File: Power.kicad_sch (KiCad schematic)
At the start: 46 parts, among them J3 DBT50G-9.5-2P, J38 2.54-1*4, J4 DBT50G-9.5-2P, J5 DBT50G-9.5-2P, J6 DBT50G-9.5-2P, U5 TPS63070RNMR

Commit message: Fix ERC: register missing libraries, add PWR_FLAGs, rename zone rails
- Register project-local sym-lib-table/fp-lib-table. PixelBlit points at
  pico-pixel's live library; RPI_COMPILED/KiCad_Standard/EasyEDA/PCM_JLCPCB
  footprints vendored (via the abandoned universal-strip-controller-first
  attempt) into libs/; RPI_DB, RPI - Power, EasyEDA, PCM_JLCPCB-Diodes and
  PCM_JLCPCB-Resistors symbols extracted from the schematics' own embedded
  symbol cache into standalone .kicad_sym files, validated with
  `kicad-cli sym upgrade`.
- Fix U1's footprint: RPI_COMPILED:rpi_rp2350b doesn't exist anywhere
  (not even in the original RP2350B-MINIMAL reference) - corrected to
  rpi_rp2350b_vias, the footprint that's actually there.
- Point D10 (BZT52C15V) and R5/R20 (0603s) at KiCad's own standard
  SOD-123/0603 footprints; no vendored copy of their original
  EasyEDA/JLCPCB footprints existed anywhere to source from.
- Add PWR_FLAGs on the 8 nets ERC found undriven: +VIN_Z1-4, +12V_SYS,
  GND (top sheet), +1V1, and VREG_AVDD (U1 pin 61).
- Rename +12V_Z1-4 to +VIN_Z1-4 (zones carry 5-12V depending on what's
  plugged in, not a fixed 12V).

ERC: 1009 violations / 8 errors -> 533 violations / 0 errors.
Remaining warnings are pre-existing: fuse/diode symbols typed
Unspecified instead of Passive (pin_to_pin), intentional dual net
labels (STRINGn/GPIOn etc., except a real USB_D+/USB_D- issue still
open), schematic drawing hygiene (off-grid/dangling wire endpoints),
and symbol-cache drift now visible now that real libraries exist
(lib_symbol_mismatch - fix via Update Symbols from Library in KiCad).
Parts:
- D10: footprint EasyEDA:SOD-123_L2.7-W1.6-LS3.7-RD-1 -> Diode_SMD:D_SOD-123
- R20, R5: footprint PCM_JLCPCB:R_0603 -> Resistor_SMD:R_0603_1608Metric
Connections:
- net +12V_Z1 renamed +VIN_Z1
- net +12V_Z2 renamed +VIN_Z2
- net +12V_Z3 renamed +VIN_Z3
- net +12V_Z4 renamed +VIN_Z4
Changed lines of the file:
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@@
 			)
 		)
-		(property "Value" "+12V_Z4"
+		(property "Value" "+VIN_Z4"
 			(at 265.684 143.002 0)
 			(show_name no)
@@
 			)
 		)
-		(property "Value" "+12V_Z2"
+		(property "Value" "+VIN_Z2"
 			(at 247.396 143.256 0)
 			(show_name no)
@@
 			)
 		)
-		(property "Value" "+12V_Z2"
+		(property "Value" "+VIN_Z2"
 			(at 180.34 99.06 0)
 			(show_name no)
@@
 			)
 		)
-		(property "Value" "+12V_Z3"
+		(property "Value" "+VIN_Z3"
 			(at 256.54 143.256 0)
 			(show_name no)
@@
 			)
 		)
-		(property "Value" "+12V_Z1"
+		(property "Value" "+VIN_Z1"
 			(at 236.982 143.51 0)
 			(show_name no)
@@
 			)
 		)
-		(property "Value" "+12V_Z2"
+		(property "Value" "+VIN_Z2"
 			(at 267.97 88.392 0)
 			(show_name no)
@@
 			)
 		)
-		(property "Value" "+12V_Z1"
+		(property "Value" "+VIN_Z1"
 			(at 242.57 88.392 0)
 			(show_name no)
@@
 			)
 		)
-		(property "Value" "+12V_Z3"
+		(property "Value" "+VIN_Z3"
 			(at 267.97 103.632 0)
 			(show_name no)
@@
 			)
 		)
-		(property "Value" "+12V_Z3"
+		(property "Value" "+VIN_Z3"
 			(at 242.57 116.332 0)
 			(show_name no)
@@
 			)
 		)
-		(property "Footprint" "EasyEDA:SOD-123_L2.7-W1.6-LS3.7-RD-1"
+		(property "Footprint" "Diode_SMD:D_SOD-123"
 			(at 25.4 50.8 0)
 			(hide yes)
@@
 			)
 		)
-		(property "Value" "+12V_Z4"
+		(property "Value" "+VIN_Z4"
 			(at 180.34 124.46 0)
 			(show_name no)
@@
 			)
 		)
-		(property "Value" "+12V_Z4"
+		(property "Value" "+VIN_Z4"
 			(at 267.97 116.332 0)
 			(show_name no)
@@
 			)
 		)
-		(property "Value" "+12V_Z1"
+		(property "Value" "+VIN_Z1"
 			(at 177.8 87.122 0)
 			(show_name no)
@@
 			)
 		)
-		(property "Footprint" "PCM_JLCPCB:R_0603"
+		(property "Footprint" "Resistor_SMD:R_0603_1608Metric"
 			(at 168.91 52.578 90)
 			(hide yes)
@@
 			)
 		)
-		(property "Value" "+12V_Z2"
+		(property "Value" "+VIN_Z2"
 			(at 242.57 103.632 0)
 			(show_name no)
@@
 	)
 	(symbol
+		(lib_id "PixelBlit:PWR_FLAG")
+		(at 38.1 48.26 90)
+		(unit 1)
+		(body_style 1)
+		(exclude_from_sim no)
+		(in_bom yes)
+		(on_board yes)
+		(in_pos_files yes)
+		(dnp no)
+		(fields_autoplaced yes)
+		(property "Reference" "#FLG23"
+			(at 36.195 48.26 0)
+			(hide yes)
+			(show_name no)
+			(do_not_autoplace no)
+			(effects
+				(font
+					(size 1.27 1.27)
+				)
+			)
+		)
+		(property "Value" "PWR_FLAG"
+			(at 34.29 48.259899999999995 90)
+			(show_name no)
+			(do_not_autoplace no)
+			(effects
+				(font
+					(size 1.27 1.27)
+				)
+				(justify left)
+			)
+		)
+		(property "Footprint" ""
+			(at 38.1 48.26 0)
+			(hide yes)
+			(show_name no)
+			(do_not_autoplace no)
+			(effects
+				(font
+					(size 1.27 1.27)
+				)
+			)
+		)
+		(property "Datasheet" ""
+			(at 38.1 48.26 0)
+			(hide yes)
+			(show_name no)
+			(do_not_autoplace no)
+			(effects
+				(font
+					(size 1.27 1.27)
+				)
+			)
+		)
+		(property "Description" "Special symbol for telling ERC where power comes from"
+			(at 38.1 48.26 0)
+			(hide yes)
+			(show_name no)
+			(do_not_autoplace no)
+			(effects
+				(font
+					(size 1.27 1.27)
+				)
+			)
+		)
+		(pin "1"
+		)
+		(instances
+			(project "universal-strip-controller"
+				(path "/b1a25501-925f-4082-acf3-9513bc59c329/b2bef3cb-9181-478c-9c64-5764e6fff4f7"
+					(reference "#FLG23")
+					(unit 1)
+				)
+			)
+		)
+	)
+	(wire
+		(pts
+			(xy 30.48 48.26) (xy 38.1 48.26)
+		)
+		(stroke
+			(width 0)
+			(type default)
+		)
+	)
+	(symbol
 		(lib_id "PixelBlit:GND")
 		(at 181.61 50.8 0)
@@
 			)
 		)
-		(property "Footprint" "PCM_JLCPCB:R_0603"
+		(property "Footprint" "Resistor_SMD:R_0603_1608Metric"
 			(at 215.9 156.718 90)
 			(hide yes)
@@
 			)
 		)
-		(property "Value" "+12V_Z3"
+		(property "Value" "+VIN_Z3"
 			(at 180.34 111.76 0)
 			(show_name no)
@@
 		)
 	)
+	(symbol
+		(lib_id "PixelBlit:PWR_FLAG")
+		(at 187.96 116.84 90)
+		(unit 1)
+		(body_style 1)
+		(exclude_from_sim no)
+		(in_bom yes)
+		(on_board yes)
+		(in_pos_files yes)
+		(dnp no)
+		(fields_autoplaced yes)
+		(property "Reference" "#FLG24"
+			(at 186.055 116.84 0)
+			(hide yes)
+			(show_name no)
+			(do_not_autoplace no)
+			(effects
+				(font
+					(size 1.27 1.27)
+				)
+			)
+		)
+		(property "Value" "PWR_FLAG"
+			(at 184.15 116.8399 90)
+			(show_name no)
+			(do_not_autoplace no)
+			(effects
+				(font
+					(size 1.27 1.27)
+				)
+				(justify left)
+			)
+		)
+		(property "Footprint" ""
+			(at 187.96 116.84 0)
+			(hide yes)
+			(show_name no)
+			(do_not_autoplace no)
+			(effects
+				(font
+					(size 1.27 1.27)
+				)
+			)
+		)
+		(property "Datasheet" ""
+			(at 187.96 116.84 0)
+			(hide yes)
+			(show_name no)
+			(do_not_autoplace no)
+			(effects
+				(font
+					(size 1.27 1.27)
+				)
+			)
+		)
+		(property "Description" "Special symbol for telling ERC where power comes from"
+			(at 187.96 116.84 0)
+			(hide yes)
+			(show_name no)
+			(do_not_autoplace no)
+			(effects
+				(font
+					(size 1.27 1.27)
+				)
+			)
+		)
+		(pin "1"
+		)
+		(instances
+			(project "universal-strip-controller"
+				(path "/b1a25501-925f-4082-acf3-9513bc59c329/b2bef3cb-9181-478c-9c64-5764e6fff4f7"
+					(reference "#FLG24")
+					(unit 1)
+				)
+			)
+		)
+	)
+	(wire
+		(pts
+			(xy 180.34 116.84) (xy 187.96 116.84)
+		)
+		(stroke
+			(width 0)
+			(type default)
+		)
+	)

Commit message: Updated symbols from library
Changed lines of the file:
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@@
 	(wire
 		(pts
+			(xy 180.34 116.84) (xy 187.96 116.84)
+		)
+		(stroke
+			(width 0)
+			(type default)
+		)
+	)
+	(wire
+		(pts
 			(xy 162.56 50.8) (xy 165.1 50.8)
 		)
@@
 	(wire
 		(pts
+			(xy 30.48 48.26) (xy 38.1 48.26)
+		)
+		(stroke
+			(width 0)
+			(type default)
+		)
+	)
+	(wire
+		(pts
 			(xy 245.11 107.95) (xy 245.11 110.49)
 		)
@@
 	)
 	(symbol
+		(lib_id "PixelBlit:PWR_FLAG")
+		(at 38.1 48.26 90)
+		(unit 1)
+		(body_style 1)
+		(exclude_from_sim no)
+		(in_bom yes)
+		(on_board yes)
+		(in_pos_files yes)
+		(dnp no)
+		(fields_autoplaced yes)
+		(property "Reference" "#FLG23"
+			(at 36.195 48.26 0)
+			(hide yes)
+			(show_name no)
+			(do_not_autoplace no)
+			(effects
+				(font
+					(size 1.27 1.27)
+				)
+			)
+		)
+		(property "Value" "PWR_FLAG"
+			(at 34.29 48.2599 90)
+			(show_name no)
+			(do_not_autoplace no)
+			(effects
+				(font
+					(size 1.27 1.27)
+				)
+				(justify left)
+			)
+		)
+		(property "Footprint" ""
+			(at 38.1 48.26 0)
+			(hide yes)
+			(show_name no)
+			(do_not_autoplace no)
+			(effects
+				(font
+					(size 1.27 1.27)
+				)
+			)
+		)
+		(property "Datasheet" ""
+			(at 38.1 48.26 0)
+			(hide yes)
+			(show_name no)
+			(do_not_autoplace no)
+			(effects
+				(font
+					(size 1.27 1.27)
+				)
+			)
+		)
+		(property "Description" "Special symbol for telling ERC where power comes from"
+			(at 38.1 48.26 0)
+			(hide yes)
+			(show_name no)
+			(do_not_autoplace no)
+			(effects
+				(font
+					(size 1.27 1.27)
+				)
+			)
+		)
+		(pin "1"
+		)
+		(instances
+			(project "universal-strip-controller"
+				(path "/b1a25501-925f-4082-acf3-9513bc59c329/b2bef3cb-9181-478c-9c64-5764e6fff4f7"
+					(reference "#FLG23")
+					(unit 1)
+				)
+			)
+		)
+	)
+	(symbol
 		(lib_id "PixelBlit:+5V")
 		(at 30.48 130.81 0)
@@
 	(symbol
 		(lib_id "PixelBlit:PWR_FLAG")
-		(at 38.1 48.26 90)
+		(at 187.96 116.84 90)
 		(unit 1)
 		(body_style 1)
@@
 		(dnp no)
 		(fields_autoplaced yes)
-		(property "Reference" "#FLG23"
-			(at 36.195 48.26 0)
+		(property "Reference" "#FLG24"
+			(at 186.055 116.84 0)
 			(hide yes)
 			(show_name no)
@@
 		)
 		(property "Value" "PWR_FLAG"
-			(at 34.29 48.259899999999995 90)
+			(at 184.15 116.8399 90)
 			(show_name no)
 			(do_not_autoplace no)
@@
 		)
 		(property "Footprint" ""
-			(at 38.1 48.26 0)
+			(at 187.96 116.84 0)
 			(hide yes)
 			(show_name no)
@@
 		)
 		(property "Datasheet" ""
-			(at 38.1 48.26 0)
+			(at 187.96 116.84 0)
 			(hide yes)
 			(show_name no)
@@
 		)
 		(property "Description" "Special symbol for telling ERC where power comes from"
-			(at 38.1 48.26 0)
+			(at 187.96 116.84 0)
 			(hide yes)
 			(show_name no)
@@
 			(project "universal-strip-controller"
 				(path "/b1a25501-925f-4082-acf3-9513bc59c329/b2bef3cb-9181-478c-9c64-5764e6fff4f7"
-					(reference "#FLG23")
+					(reference "#FLG24")
 					(unit 1)
 				)
@@
 		)
 	)
-	(wire
-		(pts
-			(xy 30.48 48.26) (xy 38.1 48.26)
-		)
-		(stroke
-			(width 0)
-			(type default)
-		)
-	)
 	(symbol
 		(lib_id "PixelBlit:GND")
@@
 		)
 	)
-	(symbol
-		(lib_id "PixelBlit:PWR_FLAG")
-		(at 187.96 116.84 90)
-		(unit 1)
-		(body_style 1)
-		(exclude_from_sim no)
-		(in_bom yes)
-		(on_board yes)
-		(in_pos_files yes)
-		(dnp no)
-		(fields_autoplaced yes)
-		(property "Reference" "#FLG24"
-			(at 186.055 116.84 0)
-			(hide yes)
-			(show_name no)
-			(do_not_autoplace no)
-			(effects
-				(font
-					(size 1.27 1.27)
-				)
-			)
-		)
-		(property "Value" "PWR_FLAG"
-			(at 184.15 116.8399 90)
-			(show_name no)
-			(do_not_autoplace no)
-			(effects
-				(font
-					(size 1.27 1.27)
-				)
-				(justify left)
-			)
-		)
-		(property "Footprint" ""
-			(at 187.96 116.84 0)
-			(hide yes)
-			(show_name no)
-			(do_not_autoplace no)
-			(effects
-				(font
-					(size 1.27 1.27)
-				)
-			)
-		)
-		(property "Datasheet" ""
-			(at 187.96 116.84 0)
-			(hide yes)
-			(show_name no)
-			(do_not_autoplace no)
-			(effects
-				(font
-					(size 1.27 1.27)
-				)
-			)
-		)
-		(property "Description" "Special symbol for telling ERC where power comes from"
-			(at 187.96 116.84 0)
-			(hide yes)
-			(show_name no)
-			(do_not_autoplace no)
-			(effects
-				(font
-					(size 1.27 1.27)
-				)
-			)
-		)
-		(pin "1"
-		)
-		(instances
-			(project "universal-strip-controller"
-				(path "/b1a25501-925f-4082-acf3-9513bc59c329/b2bef3cb-9181-478c-9c64-5764e6fff4f7"
-					(reference "#FLG24")
-					(unit 1)
-				)
-			)
-		)
-	)
-	(wire
-		(pts
-			(xy 180.34 116.84) (xy 187.96 116.84)
-		)
-		(stroke
-			(width 0)
-			(type default)
-		)
-	)

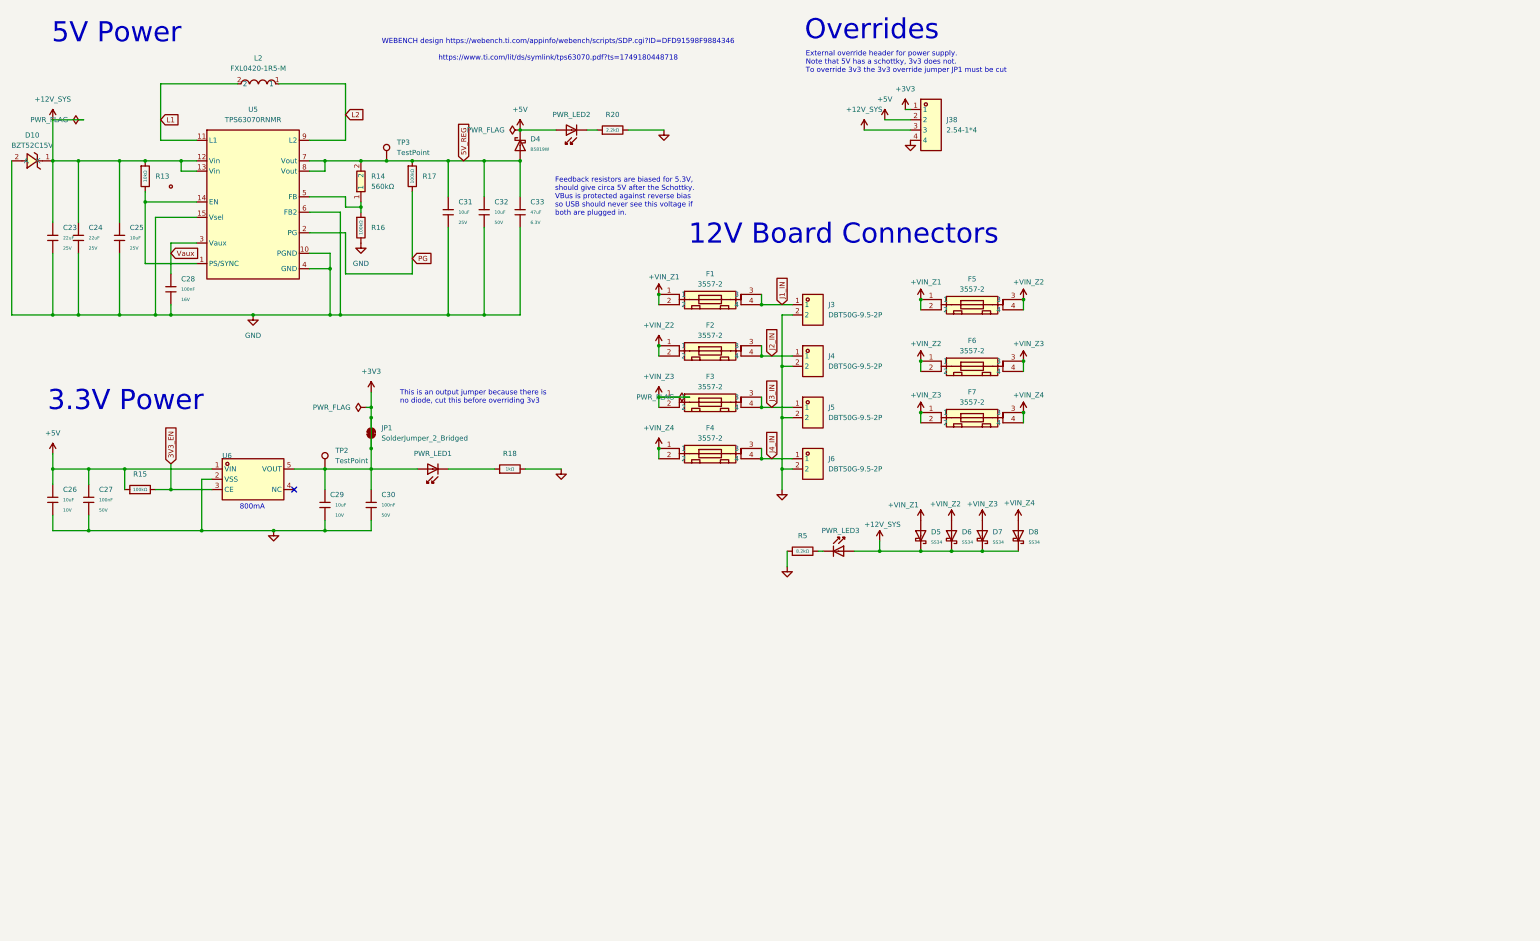
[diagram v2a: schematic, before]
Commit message: Added power sensing for each of the VIN zones
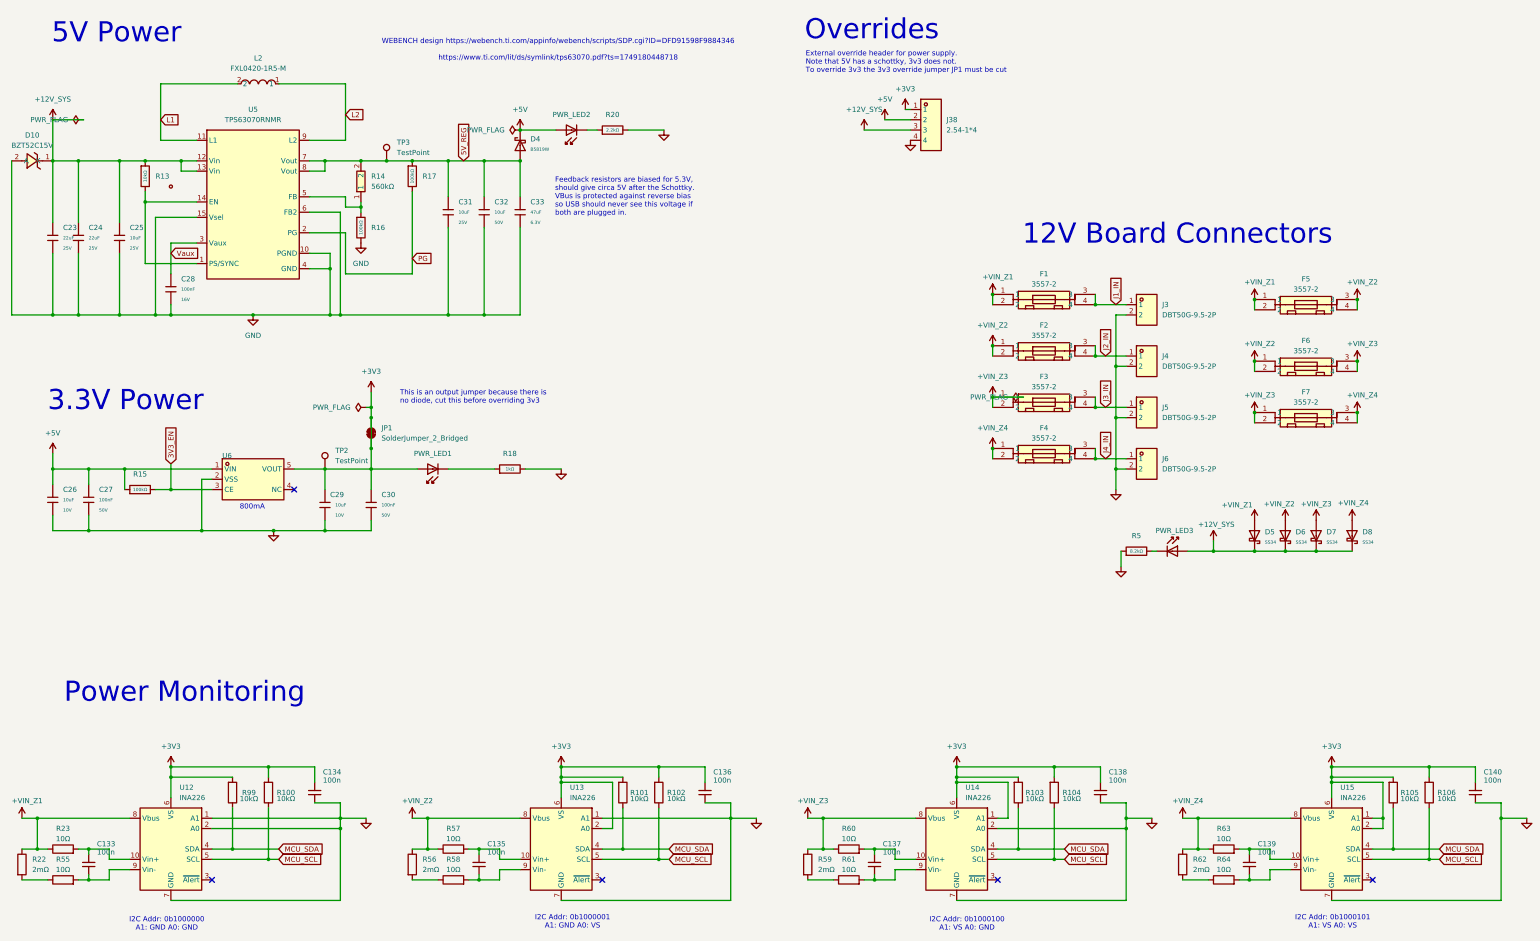
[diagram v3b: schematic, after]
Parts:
- added C133, C134, C135, C136, C137, C138, C139, C140: 100n, RPI_COMPILED:generic_capc1005x50, symbol RPI_DB:Capacitors | MLCC | M1005/RP-01BJ9Y-KRGF41
- added R100, R101, R102, R103, R104, R105, R106, R99: 10kΩ, PixelBlit:R_0603, symbol PixelBlit:0603,10kΩ
- added R22, R56, R59, R62: 2mΩ, symbol Device:R
- added R23, R55, R57, R58, R60, R61, R63, R64: 10Ω, symbol Device:R
- added U12, U13, U14, U15: INA226, Package_SO:TSSOP-10_3x3mm_P0.5mm, symbol Sensor_Energy:INA226
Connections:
- net +3V3: now also C134.1, C136.1, C138.1, C140.1, R100.1, R101.1, R102.1, R103.1, R104.1, R105.1, R106.1, R99.1, U12.6 (VS), U13.2 (A0), U13.6 (VS), U14.1 (A1), U14.6 (VS), U15.1 (A1), U15.2 (A0), U15.6 (VS)
- net +VIN_Z1: now also R22.1, R23.1, U12.8 (Vbus)
- net +VIN_Z2: now also R56.1, R57.1, U13.8 (Vbus)
- net +VIN_Z3: now also R59.1, R60.1, U14.8 (Vbus)
- net +VIN_Z4: now also R62.1, R63.1, U15.8 (Vbus)
- net GND: now also C134.2, C136.2, C138.2, C140.2, U12.1 (A1), U12.2 (A0), U12.7 (GND), U13.1 (A1), U13.7 (GND), U14.2 (A0), U14.7 (GND), U15.7 (GND)
- new net: R56.2, R58.1
- new net: C139.1, R63.2, U15.10 (Vin+)
- new net: C139.2, R64.2, U15.9 (Vin-)
- new net: C137.1, R60.2, U14.10 (Vin+)
- new net: R62.2, R64.1
- new net: C135.1, R57.2, U13.10 (Vin+)
- new net: C135.2, R58.2, U13.9 (Vin-)
- new net: C133.1, R23.2, U12.10 (Vin+)
- new net: C133.2, R55.2, U12.9 (Vin-)
- new net: R22.2, R55.1
- new net: C137.2, R61.2, U14.9 (Vin-)
- new net: R59.2, R61.1
- new net MCU_SCL: R100.2, R102.2, R104.2, R106.2, U12.5 (SCL), U13.5 (SCL), U14.5 (SCL), U15.5 (SCL)
- new net MCU_SDA: R101.2, R103.2, R105.2, R99.2, U12.4 (SDA), U13.4 (SDA), U14.4 (SDA), U15.4 (SDA)
- no-connect marks 1 -> 5
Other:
- note added: "I2C Addr: 0b1000000 A1: GND A0: GND"
- note added: "I2C Addr: 0b1000001 A1: GND A0: VS"
- note added: "I2C Addr: 0b1000100 A1: VS A0: GND"
- note added: "I2C Addr: 0b1000101 A1: VS A0: VS"
- note added: "Power Monitoring"
- moved on the sheet: D5, D6, D7, D8, F1, F2, F3, F4, F5, F6, F7, J3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
